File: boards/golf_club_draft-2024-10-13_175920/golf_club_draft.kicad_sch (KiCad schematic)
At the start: 36 parts, among them J1 USB_C_Receptacle_USB2.0_16P, Q1 PNP, Q2 NPN, Q3 PNP, U1 ICM-20948, U2 CP2104, U3 ESP32-S3-WROOM-1

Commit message: Completed first draft of PCB
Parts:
- removed C8: 1uF, Capacitor_SMD:C_0805_2012Metric_Pad1.18x1.45mm_HandSolder, symbol Device:C
- removed R2: 4k, Resistor_SMD:R_0805_2012Metric_Pad1.20x1.40mm_HandSolder, symbol Device:R
- added H1, H2, H3, H4: MountingHole, MountingHole:MountingHole_3.2mm_M3, symbol Mechanical:MountingHole
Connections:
- net GND: now also BATTCHARGER1.11 (NTC)
- net VBATT: now also BATTIO1.2 (Pin_2); no longer BATTIO1.1 (Pin_1)
- removed net BATTTHERM: BATTCHARGER1.11 (NTC), BATTIO1.2 (Pin_2)

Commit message: 3rd round PCB order revisions
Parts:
- added R10, R11, R12, R2: 10K, Resistor_SMD:R_0805_2012Metric_Pad1.20x1.40mm_HandSolder, symbol Device:R
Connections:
- net DTR: now also R2.1; no longer Q2.2 (B)
- net GND: now also J1.S1 (SHIELD)
- net GPIO0: now also R12.1; no longer Q3.1 (C)
- net RESET: now also R11.2; no longer Q2.1 (C)
- net RTS: now also R10.1; no longer Q3.2 (B)
- new net: Q3.1 (C), R12.2
- new net: Q3.2 (B), R10.2
- new net: Q2.1 (C), R11.1
- new net: Q2.2 (B), R2.2

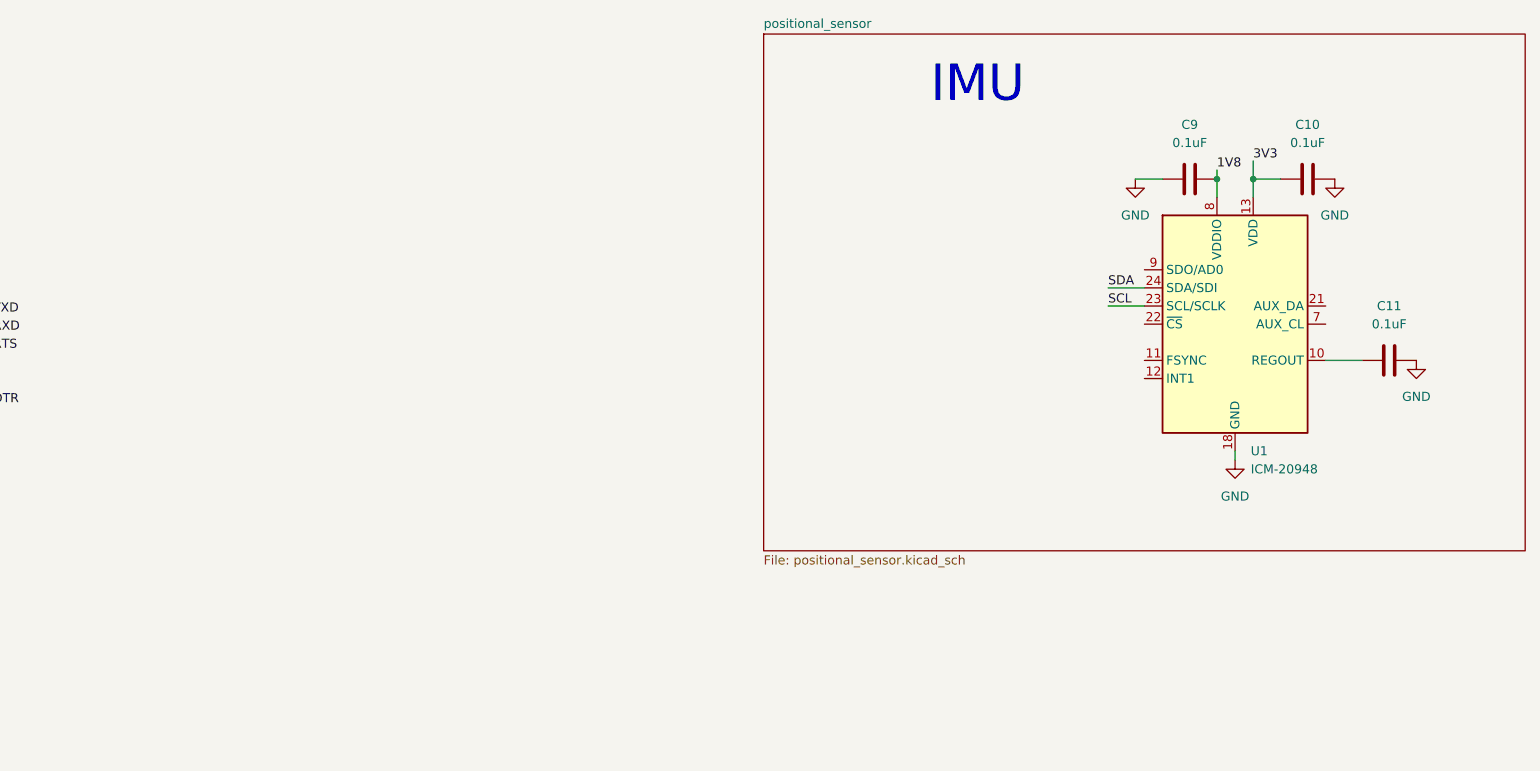
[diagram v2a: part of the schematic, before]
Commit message: Some more kicad files, round 3 and 4
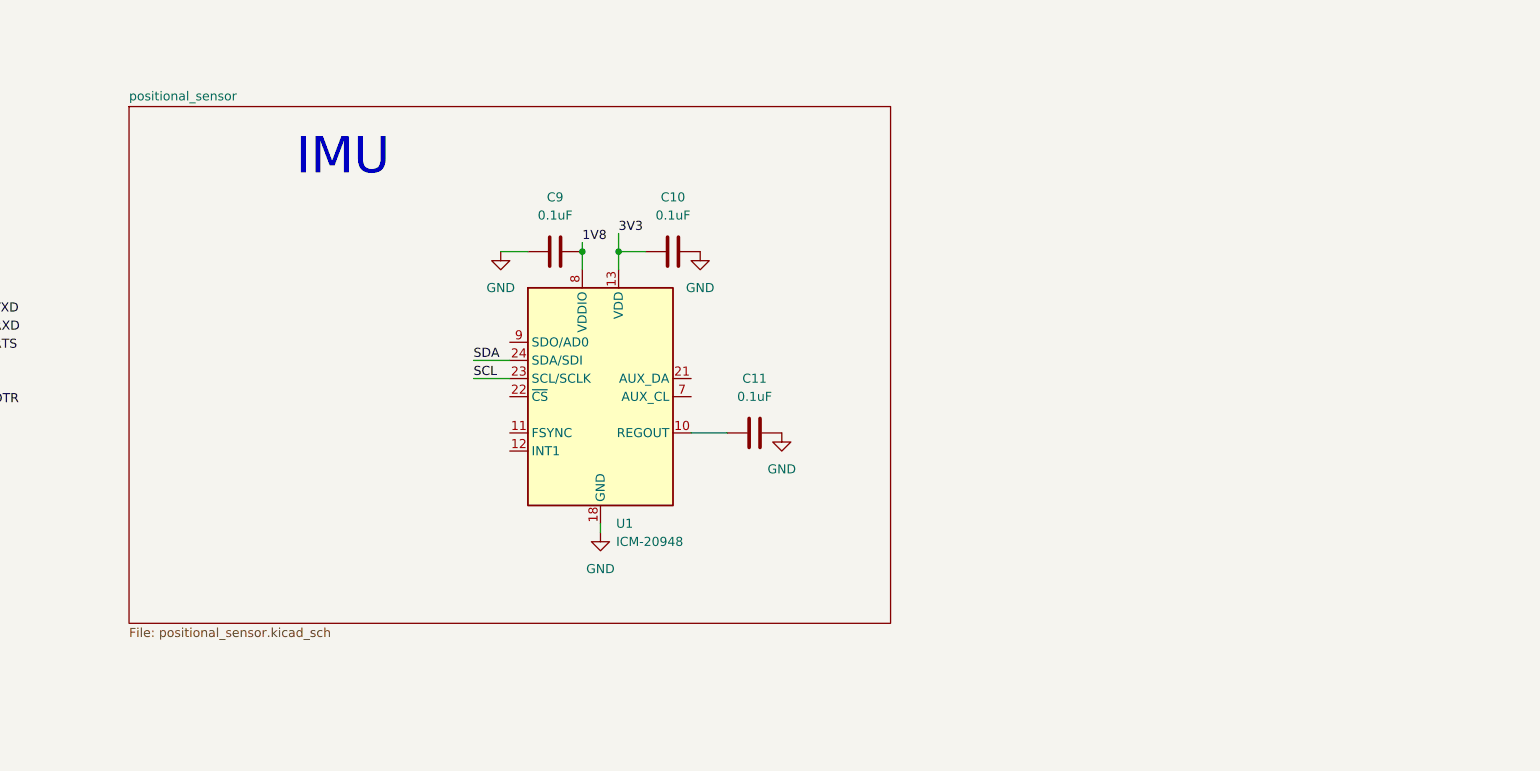
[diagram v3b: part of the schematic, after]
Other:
- moved on the sheet: C10, C11, C9, U1
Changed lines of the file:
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@@
 	)
 	(junction
-		(at 449.58 20.32)
+		(at 360.68 30.48)
 		(diameter 0)
 		(color 0 0 0 0)
@@
 	)
 	(junction
-		(at 444.5 20.32)
+		(at 355.6 30.48)
 		(diameter 0)
 		(color 0 0 0 0)
@@
 	(wire
 		(pts
-			(xy 433.07 20.32) (xy 436.88 20.32)
+			(xy 344.17 30.48) (xy 347.98 30.48)
 		)
 		(stroke
@@
 	(wire
 		(pts
-			(xy 444.5 20.32) (xy 444.5 22.86)
+			(xy 355.6 30.48) (xy 355.6 33.02)
 		)
 		(stroke
@@
 	(wire
 		(pts
-			(xy 429.26 38.1) (xy 434.34 38.1)
+			(xy 340.36 48.26) (xy 345.44 48.26)
 		)
 		(stroke
@@
 	(wire
 		(pts
-			(xy 459.74 45.72) (xy 464.82 45.72)
+			(xy 370.84 55.88) (xy 375.92 55.88)
 		)
 		(stroke
@@
 	(wire
 		(pts
-			(xy 429.26 35.56) (xy 434.34 35.56)
+			(xy 340.36 45.72) (xy 345.44 45.72)
 		)
 		(stroke
@@
 	(wire
 		(pts
-			(xy 444.5 19.05) (xy 444.5 20.32)
+			(xy 355.6 29.21) (xy 355.6 30.48)
 		)
 		(stroke
@@
 	(wire
 		(pts
-			(xy 449.58 20.32) (xy 453.39 20.32)
+			(xy 360.68 30.48) (xy 364.49 30.48)
 		)
 		(stroke
@@
 	(wire
 		(pts
-			(xy 447.04 58.42) (xy 447.04 59.69)
+			(xy 358.14 68.58) (xy 358.14 69.85)
 		)
 		(stroke
@@
 	(wire
 		(pts
-			(xy 449.58 17.78) (xy 449.58 20.32)
+			(xy 360.68 27.94) (xy 360.68 30.48)
 		)
 		(stroke
@@
 	(wire
 		(pts
-			(xy 449.58 20.32) (xy 449.58 22.86)
+			(xy 360.68 30.48) (xy 360.68 33.02)
 		)
 		(stroke
@@
 	(text "IMU"
 		(exclude_from_sim no)
-		(at 410.972 7.112 0)
+		(at 322.072 17.272 0)
 		(effects
 			(font
@@
 	)
 	(label "1V8"
-		(at 444.5 19.05 0)
+		(at 355.6 29.21 0)
 		(fields_autoplaced yes)
 		(effects
@@
 	)
 	(label "SDA"
-		(at 429.26 35.56 0)
+		(at 340.36 45.72 0)
 		(fields_autoplaced yes)
 		(effects
@@
 	)
 	(label "SCL"
-		(at 429.26 38.1 0)
+		(at 340.36 48.26 0)
 		(fields_autoplaced yes)
 		(effects
@@
 	)
 	(label "3V3"
-		(at 449.58 17.78 0)
+		(at 360.68 27.94 0)
 		(fields_autoplaced yes)
 		(effects
@@
 	(symbol
 		(lib_id "power:GND")
-		(at 461.01 20.32 0)
+		(at 372.11 30.48 0)
 		(unit 1)
 		(exclude_from_sim no)
@@
 		(fields_autoplaced yes)
 		(property "Reference" "#PWR026"
-			(at 461.01 26.67 0)
+			(at 372.11 36.83 0)
 			(effects
 				(font
@@
 		)
 		(property "Value" "GND"
-			(at 461.01 25.4 0)
+			(at 372.11 35.56 0)
 			(effects
 				(font
@@
 		)
 		(property "Footprint" ""
-			(at 461.01 20.32 0)
+			(at 372.11 30.48 0)
 			(effects
 				(font
@@
 		)
 		(property "Datasheet" ""
-			(at 461.01 20.32 0)
+			(at 372.11 30.48 0)
 			(effects
 				(font
@@
 		)
 		(property "Description" "Power symbol creates a global label with name \"GND\" , ground"
-			(at 461.01 20.32 0)
+			(at 372.11 30.48 0)
 			(effects
 				(font
@@
 	(symbol
 		(lib_id "Device:C")
-		(at 457.2 20.32 90)
+		(at 368.3 30.48 90)
 		(unit 1)
 		(exclude_from_sim no)
@@
 		(fields_autoplaced yes)
 		(property "Reference" "C10"
-			(at 457.2 12.7 90)
+			(at 368.3 22.86 90)
 			(effects
 				(font
@@
 		)
 		(property "Value" "0.1uF"
-			(at 457.2 15.24 90)
+			(at 368.3 25.4 90)
 			(effects
 				(font
@@
 		)
 		(property "Footprint" "Capacitor_SMD:C_0805_2012Metric_Pad1.18x1.45mm_HandSolder"
-			(at 461.01 19.3548 0)
+			(at 372.11 29.5148 0)
 			(effects
 				(font
@@
 		)
 		(property "Datasheet" "~"
-			(at 457.2 20.32 0)
+			(at 368.3 30.48 0)
 			(effects
 				(font
@@
 		)
 		(property "Description" "Unpolarized capacitor"
-			(at 457.2 20.32 0)
+			(at 368.3 30.48 0)
 			(effects
 				(font
@@
 	(symbol
 		(lib_id "Device:C")
-		(at 468.63 45.72 90)
+		(at 379.73 55.88 90)
 		(unit 1)
 		(exclude_from_sim no)
@@
 		(fields_autoplaced yes)
 		(property "Reference" "C11"
-			(at 468.63 38.1 90)
+			(at 379.73 48.26 90)
 			(effects
 				(font
@@
 		)
 		(property "Value" "0.1uF"
-			(at 468.63 40.64 90)
+			(at 379.73 50.8 90)
 			(effects
 				(font
@@
 		)
 		(property "Footprint" "Capacitor_SMD:C_0805_2012Metric_Pad1.18x1.45mm_HandSolder"
-			(at 472.44 44.7548 0)
+			(at 383.54 54.9148 0)
 			(effects
 				(font
@@
 		)
 		(property "Datasheet" "~"
-			(at 468.63 45.72 0)
+			(at 379.73 55.88 0)
 			(effects
 				(font
@@
 		)
 		(property "Description" "Unpolarized capacitor"
-			(at 468.63 45.72 0)
+			(at 379.73 55.88 0)
 			(effects
 				(font
@@
 	(symbol
 		(lib_id "power:GND")
-		(at 433.07 20.32 0)
+		(at 344.17 30.48 0)
 		(unit 1)
 		(exclude_from_sim no)
@@
 		(fields_autoplaced yes)
 		(property "Reference" "#PWR020"
-			(at 433.07 26.67 0)
+			(at 344.17 36.83 0)
 			(effects
 				(font
@@
 		)
 		(property "Value" "GND"
-			(at 433.07 25.4 0)
+			(at 344.17 35.56 0)
 			(effects
 				(font
@@
 		)
 		(property "Footprint" ""
-			(at 433.07 20.32 0)
+			(at 344.17 30.48 0)
 			(effects
 				(font
@@
 		)
 		(property "Datasheet" ""
-			(at 433.07 20.32 0)
+			(at 344.17 30.48 0)
 			(effects
 				(font
@@
 		)
 		(property "Description" "Power symbol creates a global label with name \"GND\" , ground"
-			(at 433.07 20.32 0)
+			(at 344.17 30.48 0)
 			(effects
 				(font
@@
 	(symbol
 		(lib_id "power:GND")
-		(at 472.44 45.72 0)
+		(at 383.54 55.88 0)
 		(unit 1)
 		(exclude_from_sim no)
@@
 		(fields_autoplaced yes)
 		(property "Reference" "#PWR027"
-			(at 472.44 52.07 0)
+			(at 383.54 62.23 0)
 			(effects
 				(font
@@
 		)
 		(property "Value" "GND"
-			(at 472.44 50.8 0)
+			(at 383.54 60.96 0)
 			(effects
 				(font
@@
 		)
 		(property "Footprint" ""
-			(at 472.44 45.72 0)
+			(at 383.54 55.88 0)
 			(effects
 				(font
@@
 		)
 		(property "Datasheet" ""
-			(at 472.44 45.72 0)
+			(at 383.54 55.88 0)
 			(effects
 				(font
@@
 		)
 		(property "Description" "Power symbol creates a global label with name \"GND\" , ground"
-			(at 472.44 45.72 0)
+			(at 383.54 55.88 0)
 			(effects
 				(font
@@
 	(symbol
 		(lib_id "Sensor_Motion:ICM-20948")
-		(at 447.04 40.64 0)
+		(at 358.14 50.8 0)
 		(unit 1)
 		(exclude_from_sim no)
@@
 		(fields_autoplaced yes)
 		(property "Reference" "U1"
-			(at 449.2341 58.42 0)
+			(at 360.3341 68.58 0)
 			(effects
 				(font
@@
 		)
 		(property "Value" "ICM-20948"
-			(at 449.2341 60.96 0)
+			(at 360.3341 71.12 0)
 			(effects
 				(font
@@
 		)
 		(property "Footprint" "Sensor_Motion:InvenSense_QFN-24_3x3mm_P0.4mm"
-			(at 447.04 66.04 0)
+			(at 358.14 76.2 0)
 			(effects
 				(font
@@
 		)
 		(property "Datasheet" "http://www.invensense.com/wp-content/uploads/2016/06/DS-000189-ICM-20948-v1.3.pdf"
-			(at 447.04 44.45 0)
+			(at 358.14 54.61 0)
 			(effects
 				(font
@@
 		)
 		(property "Description" "InvenSense 9-Axis Motion Sensor, Accelerometer, Gyroscope, Compass, I2C/SPI, QFN-24"
-			(at 447.04 40.64 0)
+			(at 358.14 50.8 0)
 			(effects
 				(font
@@
 	(symbol
 		(lib_id "Device:C")
-		(at 440.69 20.32 90)
+		(at 351.79 30.48 90)
 		(unit 1)
 		(exclude_from_sim no)
@@
 		(fields_autoplaced yes)
 		(property "Reference" "C9"
-			(at 440.69 12.7 90)
+			(at 351.79 22.86 90)
 			(effects
 				(font
@@
 		)
 		(property "Value" "0.1uF"
-			(at 440.69 15.24 90)
+			(at 351.79 25.4 90)
 			(effects
 				(font
@@
 		)
 		(property "Footprint" "Capacitor_SMD:C_0805_2012Metric_Pad1.18x1.45mm_HandSolder"
-			(at 444.5 19.3548 0)
+			(at 355.6 29.5148 0)
 			(effects
 				(font
@@
 		)
 		(property "Datasheet" "~"
-			(at 440.69 20.32 0)
+			(at 351.79 30.48 0)
 			(effects
 				(font
@@
 		)
 		(property "Description" "Unpolarized capacitor"
-			(at 440.69 20.32 0)
+			(at 351.79 30.48 0)
 			(effects
 				(font
@@
 	(symbol
 		(lib_id "power:GND")
-		(at 447.04 59.69 0)
+		(at 358.14 69.85 0)
 		(unit 1)
 		(exclude_from_sim no)
@@
 		(fields_autoplaced yes)
 		(property "Reference" "#PWR025"
-			(at 447.04 66.04 0)
+			(at 358.14 76.2 0)
 			(effects
 				(font
@@
 		)
 		(property "Value" "GND"
-			(at 447.04 64.77 0)
+			(at 358.14 74.93 0)
 			(effects
 				(font
@@
 		)
 		(property "Footprint" ""
-			(at 447.04 59.69 0)
+			(at 358.14 69.85 0)
 			(effects
 				(font
@@
 		)
 		(property "Datasheet" ""
-			(at 447.04 59.69 0)
+			(at 358.14 69.85 0)
 			(effects
 				(font
@@
 		)
 		(property "Description" "Power symbol creates a global label with name \"GND\" , ground"
-			(at 447.04 59.69 0)
+			(at 358.14 69.85 0)
 			(effects
 				(font
@@
 	)
 	(sheet
-		(at 381 0)
+		(at 292.1 10.16)
 		(size 106.68 72.39)
 		(fields_autoplaced yes)
@@
 		)
 		(property "Sheetname" "positional_sensor"
-			(at 381 -0.7116 0)
+			(at 292.1 9.4484 0)
 			(effects
 				(font
@@
 		)
 		(property "Sheetfile" "positional_sensor.kicad_sch"
-			(at 381 72.9746 0)
+			(at 292.1 83.1346 0)
 			(effects
 				(font
